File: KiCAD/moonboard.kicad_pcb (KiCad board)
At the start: 2 copper layers, 99.5 x 70.5 mm, 18 parts, among them J1 Conn_01x04_Pin, J2 Conn_01x08_Pin, SW1 SW_Push_45deg, SW2 SW_Push_45deg, SW3 SW_Push_45deg, SW4 SW_Push_45deg, SW5 SW_Push_45deg, SW6 SW_Push_45deg, U1 XIAO-ESP32-C3-SMD, U2 DHT11

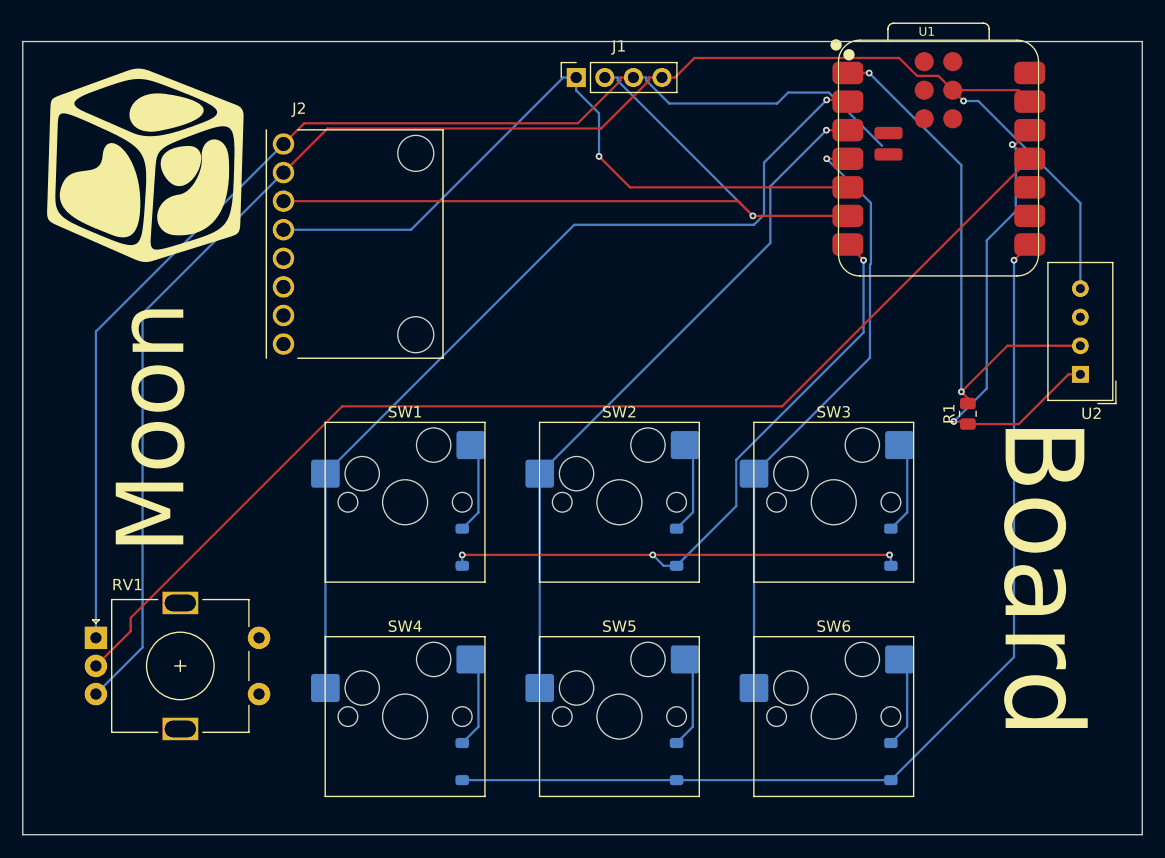
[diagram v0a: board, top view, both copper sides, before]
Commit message: Rerouted
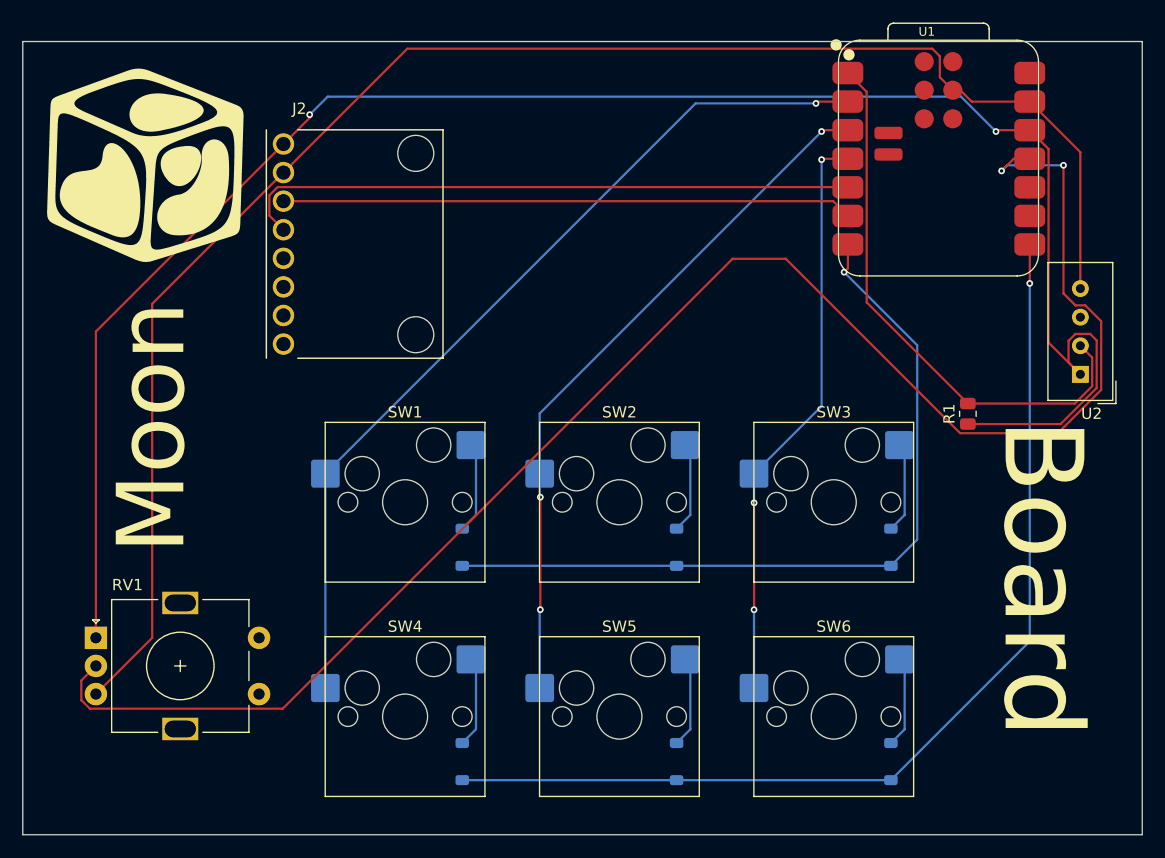
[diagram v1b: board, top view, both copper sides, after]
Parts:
- removed J1: Conn_01x04_Pin, FootprintsnModels:OLED_SSD1306_I2C_0.96
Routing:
- net /POT_IN: track 102.4 -> 149.6 mm, vias 0 -> 2
- net /SCL: track 69.1 -> 50.7 mm, vias 1 -> 0
- net +3V3: track 152.4 -> 167.3 mm
- net /ROW0: track 78.5 -> 70.5 mm, vias 4 -> 1
- net /SDA: track 62.7 -> 55.3 mm, vias 1 -> 0
- net /COL2: track 54.9 -> 51.8 mm, vias 1 -> 3
- net GND: track 148.7 -> 145.7 mm, vias 1 -> 0
- net /COL0: track 82.0 -> 79.2 mm
- net /DHT11_DATA: track 47.2 -> 49.5 mm, vias 2 -> 0
- net /COL1: track 62.0 -> 62.3 mm, vias 1 -> 3
